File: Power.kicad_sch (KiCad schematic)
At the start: 51 parts, among them U1 TVS2200DRV, U2 LT8612, U3 LT3652

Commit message: solar charger
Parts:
- R7: value R -> 10k
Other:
- note removed: "Direct Charging for batteries"

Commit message: solarcharger
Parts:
- U3: footprint (none) -> LT3652IMSE:MSOP-12_MSE_LIT
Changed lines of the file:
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@@
 			)
 		)
-		(property "Footprint" ""
+		(property "Footprint" "LT3652IMSE:MSOP-12_MSE_LIT"
 			(at 250.19 153.34 0)
 			(hide yes)

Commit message: adding more footprints
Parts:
- C12: footprint Capacitor_1uF_X7R_50V:CAP_CL31_SAM -> Capacitor_SMD:C_0805_2012Metric
- C13, C15, C5, C7: footprint Capacitor_10uF_X7R:CAP_CL32_SAM -> Capacitor_SMD:C_1210_3225Metric
- C14: footprint Cap10nFX7R:CAP_CL21_SAM -> Capacitor_SMD:C_0805_2012Metric
- C2: footprint Cap_X5R_10nF:CAP_X7R_0805_AVX -> Capacitor_SMD:C_0805_2012Metric
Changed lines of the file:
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@@
 			)
 		)
-		(property "Footprint" "Capacitor_10uF_X7R:CAP_CL32_SAM"
+		(property "Footprint" "Capacitor_SMD:C_1210_3225Metric"
 			(at 300.6852 80.01 0)
 			(hide yes)
@@
 			)
 		)
-		(property "Footprint" "Capacitor_10uF_X7R:CAP_CL32_SAM"
+		(property "Footprint" "Capacitor_SMD:C_1210_3225Metric"
 			(at 152.4 66.04 0)
 			(hide yes)
@@
 			)
 		)
-		(property "Footprint" "Capacitor_10uF_X7R:CAP_CL32_SAM"
+		(property "Footprint" "Capacitor_SMD:C_1210_3225Metric"
 			(at 193.3448 67.31 0)
 			(hide yes)
@@
 			)
 		)
-		(property "Footprint" "Capacitor_1uF_X7R_50V:CAP_CL31_SAM"
+		(property "Footprint" "Capacitor_SMD:C_0805_2012Metric"
 			(at 257.5052 55.88 0)
 			(hide yes)
@@
 			)
 		)
-		(property "Footprint" "Capacitor_10uF_X7R:CAP_CL32_SAM"
+		(property "Footprint" "Capacitor_SMD:C_1210_3225Metric"
 			(at 324.8152 74.93 0)
 			(hide yes)
@@
 			)
 		)
-		(property "Footprint" "Cap_X5R_10nF:CAP_X7R_0805_AVX"
+		(property "Footprint" "Capacitor_SMD:C_0805_2012Metric"
 			(at 123.4948 337.82 0)
 			(hide yes)
@@
 			)
 		)
-		(property "Footprint" "Cap10nFX7R:CAP_CL21_SAM"
+		(property "Footprint" "Capacitor_SMD:C_0805_2012Metric"
 			(at 317.1952 74.93 0)
 			(hide yes)

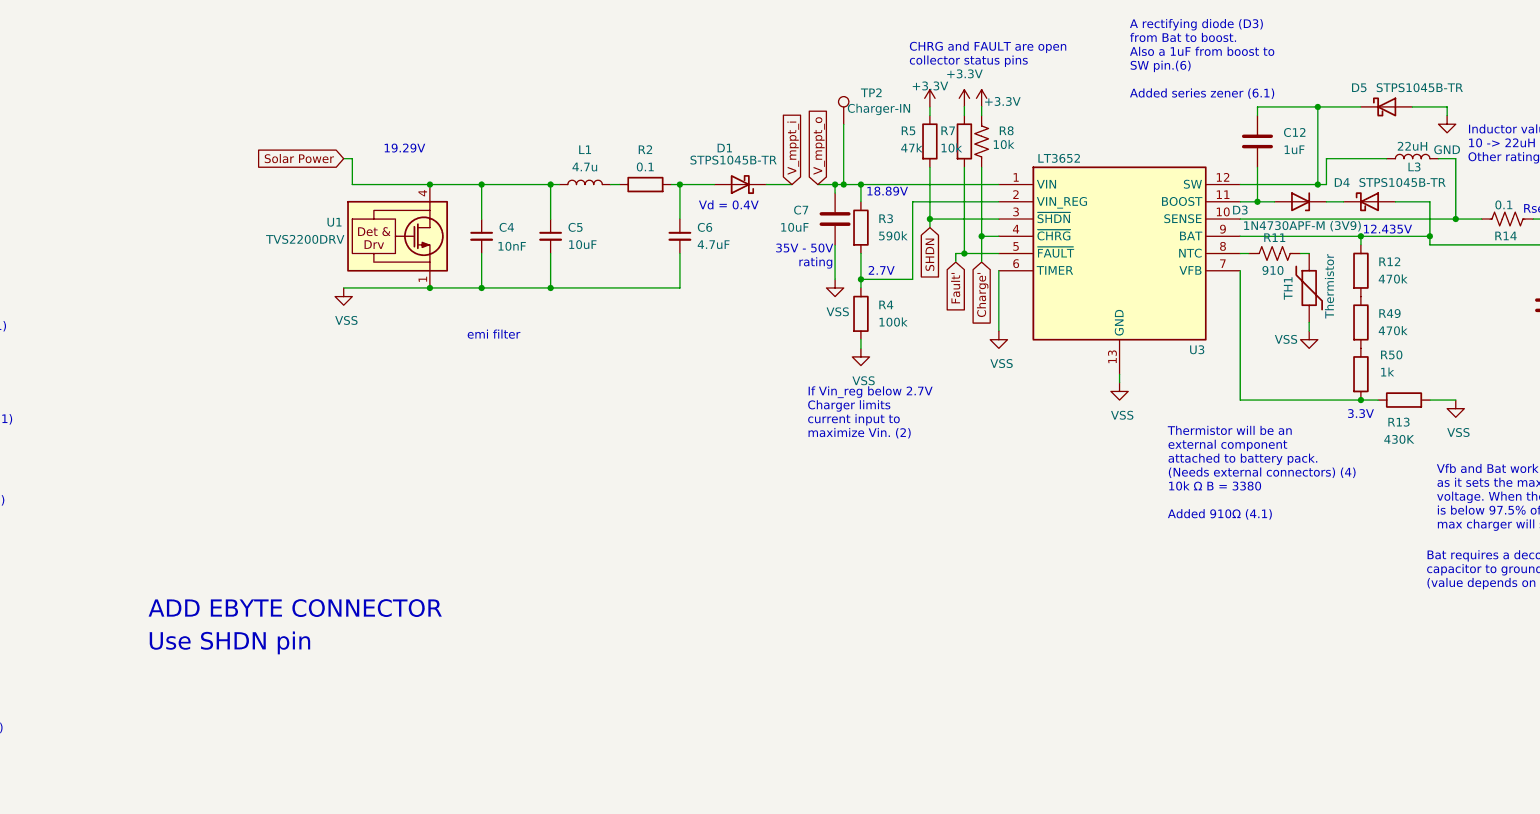
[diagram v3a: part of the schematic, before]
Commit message: Solar charger footprints
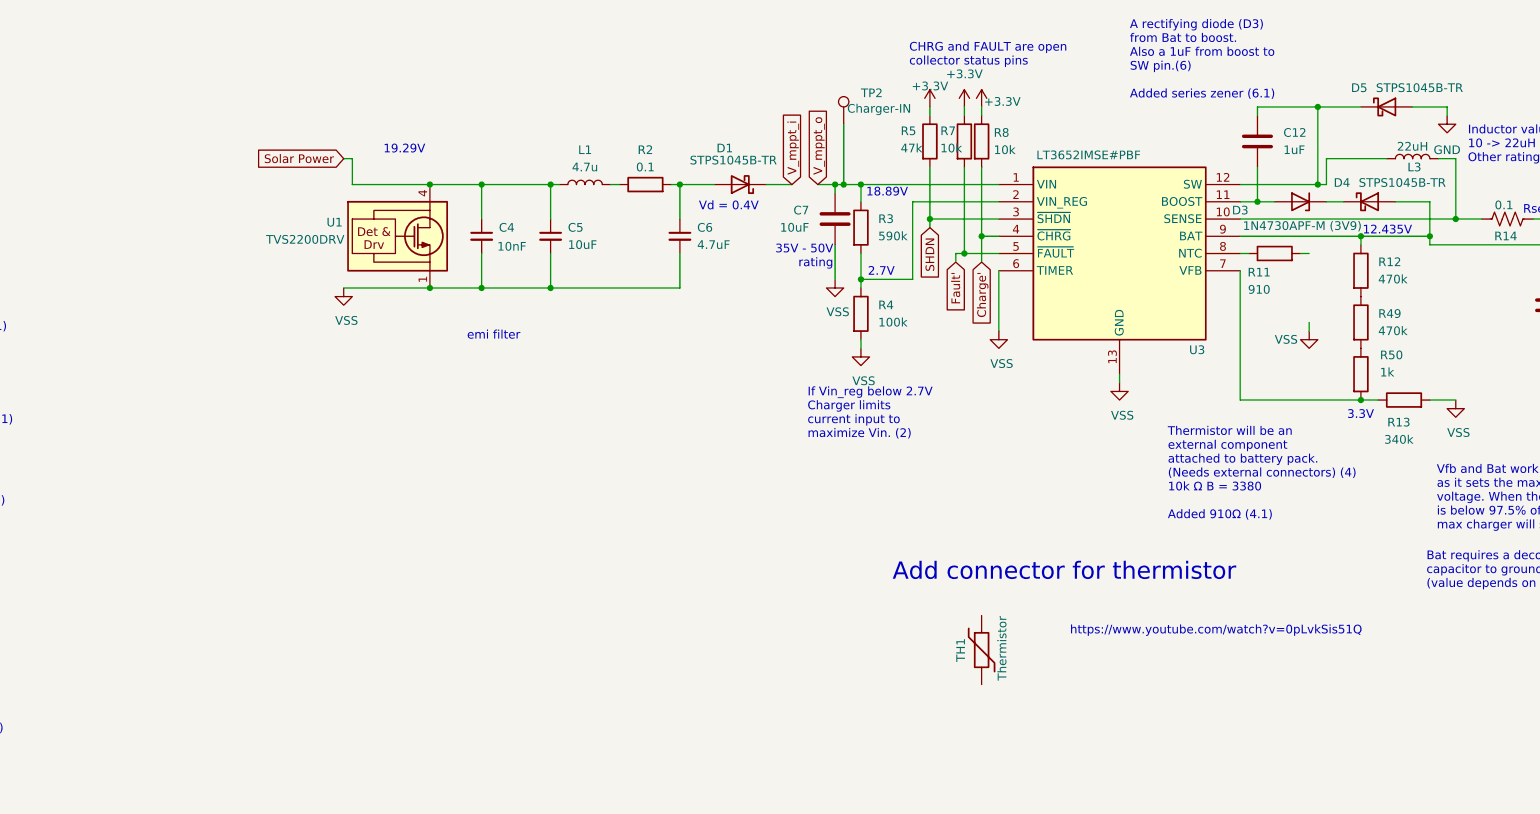
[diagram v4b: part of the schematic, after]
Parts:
- removed R11: 910, symbol Device:R_US
- removed R8: 10k, symbol Device:R_US
- added R11: 910, Resistor_SMD:R_0603_1608Metric, symbol Device:R
- added R8: 10k, Resistor_SMD:R_1210_3225Metric, symbol Device:R
- R12, R49, R50: footprint (none) -> Resistor_SMD:R_2512_6332Metric
- R13: value 430K -> 340k; footprint (none) -> Resistor_SMD:R_1206_3216Metric
- R15, R5, R7: footprint (none) -> Resistor_SMD:R_1210_3225Metric
- R3: footprint (none) -> Resistor_SMD:R_0402_1005Metric_Pad0.72x0.64mm_HandSolder
- R4: footprint (none) -> Resistor_SMD:R_1206_3216Metric
- U3: value LT3652 -> LT3652IMSE#PBF
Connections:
- net +3.3V: now also R8.1
- net Charge': now also R8.2
- net VSS: no longer TH1.2
- net at U3.8 (NTC): now also R11.1
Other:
- note added: "Add connector for thermistor"
- note added: "https://www.youtube.com/watch?v=0pLvkSis51Q"
- note removed: "ADD EBYTE CONNECTOR"
- note removed: "Use SHDN pin"

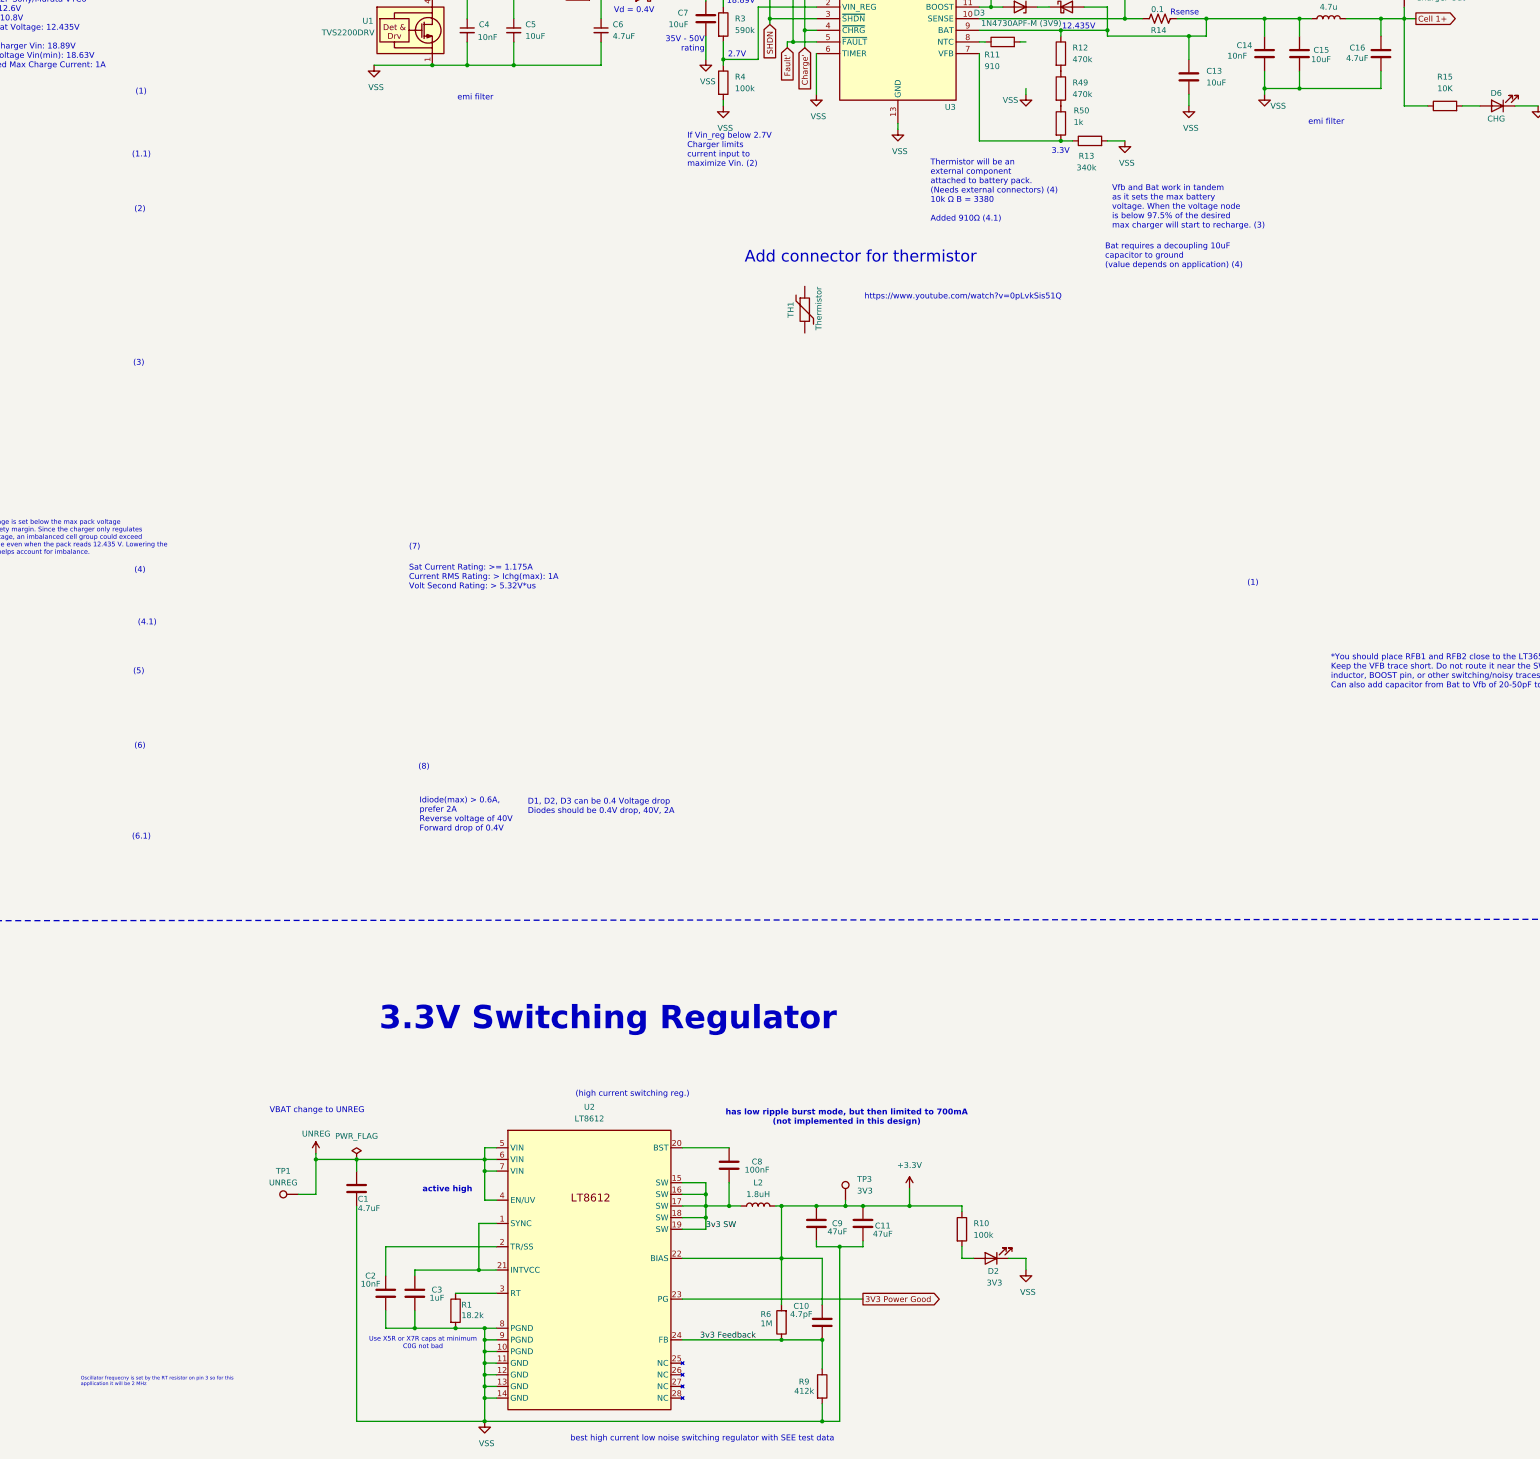
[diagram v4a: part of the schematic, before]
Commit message: Adding in EMI and GND ties
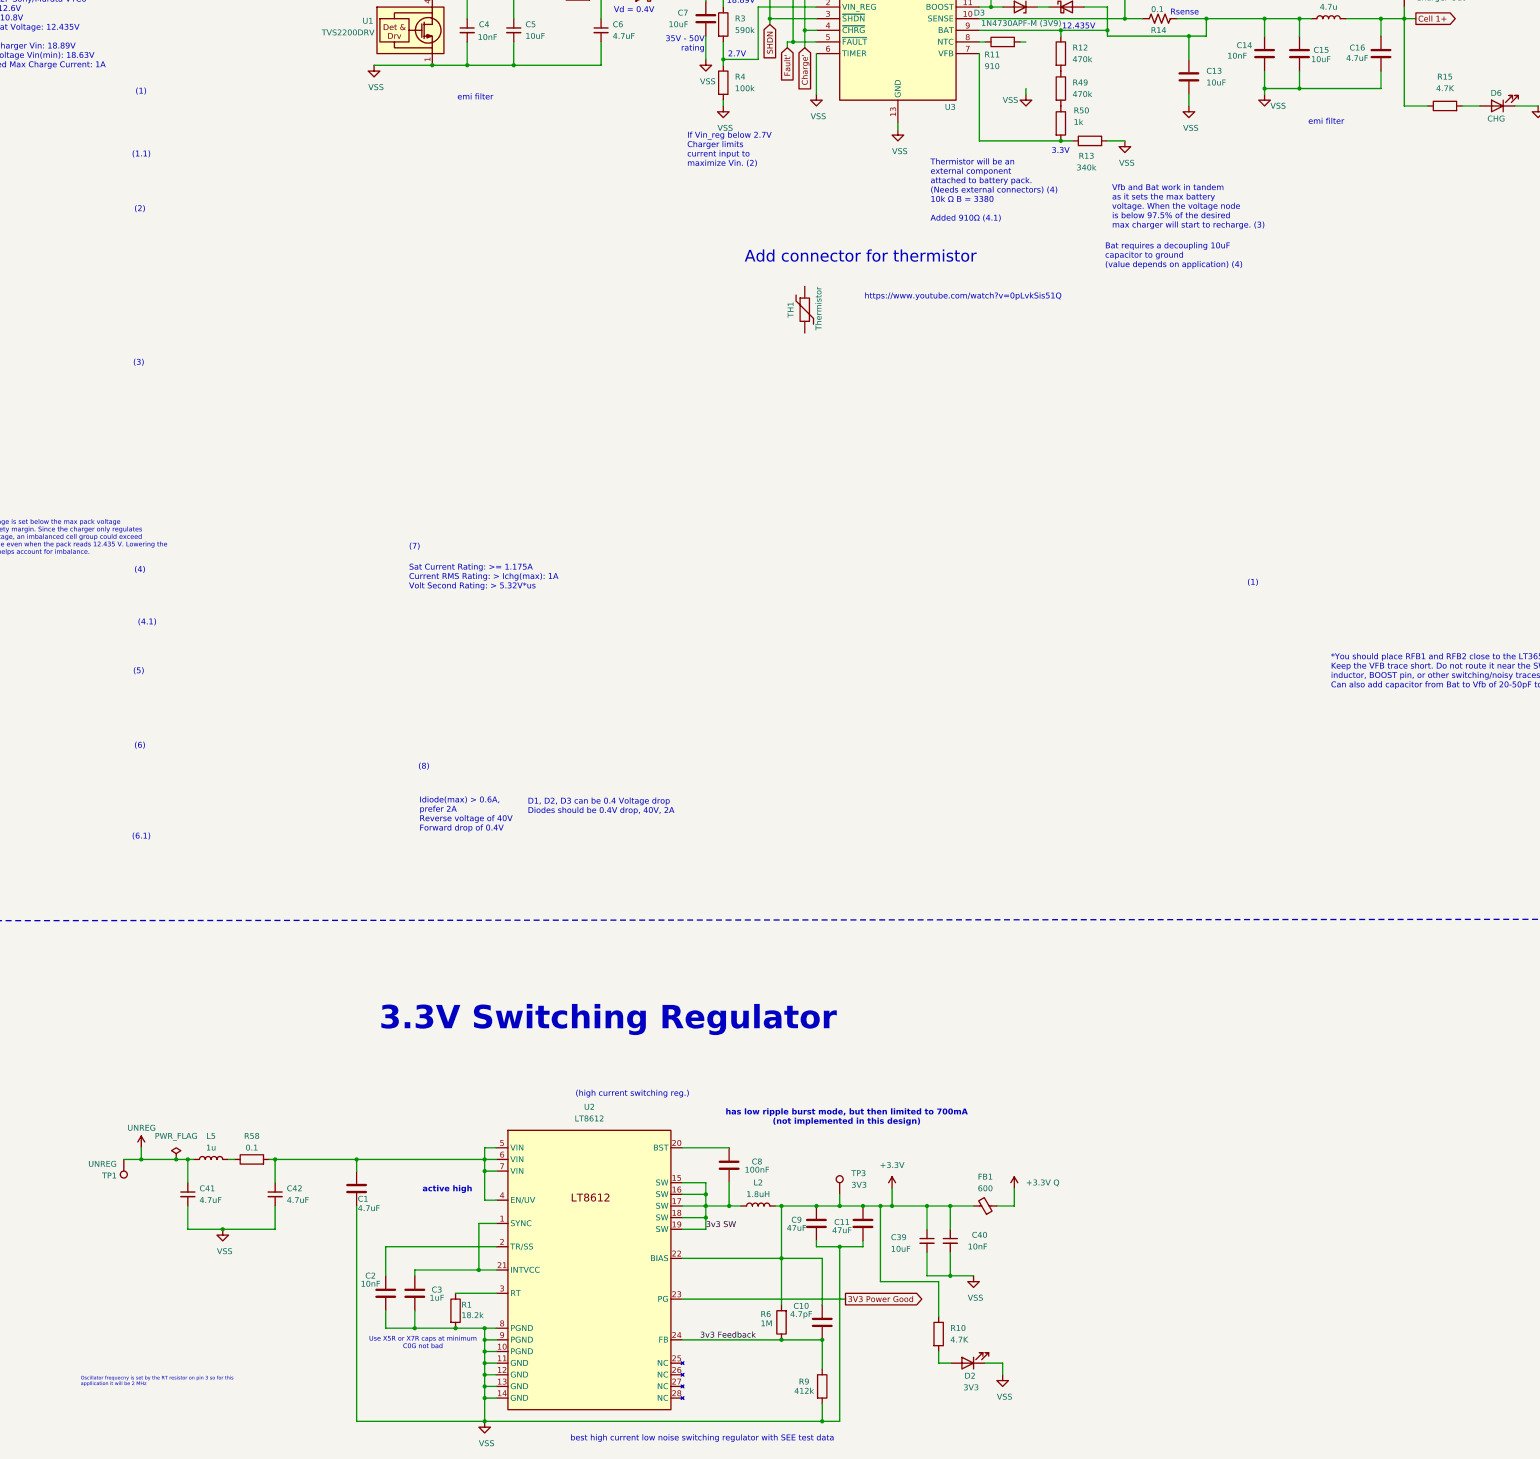
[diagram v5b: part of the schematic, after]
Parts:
- added C39: 10uF, symbol Device:C_Small
- added C40: 10nF, symbol Device:C_Small
- added C41, C42: 4.7uF, symbol Device:C_Small
- added FB1: 600, symbol Device:FerriteBead_Small
- added L5: 1u, symbol Device:L
- added R58: 0.1, symbol Device:R
- R10: value 100k -> 4.7K
- R15: value 10K -> 4.7K
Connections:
- net +3.3V: now also C39.1, C40.1, FB1.2
- net UNREG: now also C41.1, L5.1; no longer C1.1, U2.4 (EN/UV), U2.5 (VIN), U2.6 (VIN), U2.7 (VIN)
- net VSS: now also C39.2, C40.2, C41.2, C42.2
- new net: L5.2, R58.1
- new net: C1.1, C42.1, R58.2, U2.4 (EN/UV), U2.5 (VIN), U2.6 (VIN), U2.7 (VIN)
- new net +3.3V Q: FB1.1
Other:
- note removed: "VBAT change to UNREG"
- moved on the sheet: D2, R10, TP1, TP3

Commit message: Adjusting values
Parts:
- L5: value 1u -> 1uH
- R15: value 4.7K -> 10K
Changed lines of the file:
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@@
 			)
 		)
-		(property "Value" "4.7K"
+		(property "Value" "10K"
 			(at 355.6 78.74 90)
 			(show_name no)
@@
 			)
 		)
-		(property "Value" "1u"
+		(property "Value" "1uH"
 			(at 86.36 309.88 90)
 			(show_name no)
